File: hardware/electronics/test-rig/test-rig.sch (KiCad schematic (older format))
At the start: 59 parts, among them IC1 23LC1024, J1 JUMPER_OPEN, J2 JUMPER_CLOSED, J3 JUMPER_CLOSED, J4 AudioJack3_Ground, J5 Screw_Terminal_1x02, J6 Screw_Terminal_1x02, P1 CONN_01X15, P2 CONN_01X15, P3 CONN_01X04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

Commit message: Test rig
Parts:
- removed C14, C4, C5: 10u, symbol modular-internet-radio:CP_Small
- removed C24: 1u, symbol modular-internet-radio:C_Small
- removed L1, L2: Ferrite, symbol modular-internet-radio:Ferrite_Bead_Small
- added C14, C4, C5: 10u, Capacitors_SMD:C_0805_HandSoldering, symbol modular-internet-radio:C_Small
- C1, C10, C11, C12, C13, C16, C17, C18, C2, C20, C21, C3, C6, C7, C8, C9: footprint (none) -> Capacitors_SMD:C_0805_HandSoldering
- C15, C19, C22, C23: footprint (none) -> Capacitors_Tantalum_SMD:CP_Tantalum_Case-D_EIA-7343-31_Hand
- IC1: footprint DIL -> (none)
- P1, P2: footprint (none) -> Pin_Headers:Pin_Header_Straight_1x15_Pitch2.54mm
- P3, P4: footprint (none) -> Pin_Headers:Pin_Header_Straight_1x04_Pitch2.54mm
- P5, P6: footprint (none) -> Pin_Headers:Pin_Header_Straight_1x14_Pitch2.54mm
- P7: footprint (none) -> Pin_Headers:Pin_Header_Straight_1x01_Pitch2.54mm
- R1, R10, R11, R12, R13, R2, R3, R4, R5, R6, R7, R8, R9: footprint (none) -> Resistors_SMD:R_0805_HandSoldering
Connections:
- wire segments 300 -> 295
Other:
- note added: "+3.3V"
- note added: "AGND"
- note added: "AVDD"
- note added: "Ferrite"
- note added: "GND"
- note added: "Note 1: Removing the ferrite power decoupling (as in the Aadafruit design) and will try\n with partitioning of the ground and power planes."
- note added: "Note 2: Removed 1uF decoupling cap between AVDD and AGND (as per Adafruit\ndesign) as this covered by 10uF decoupling cap (as per manufacturer reference design)"
- note added: "See Note 1"
- note removed: "RESET JUMPER??"
- moved on the sheet: P2

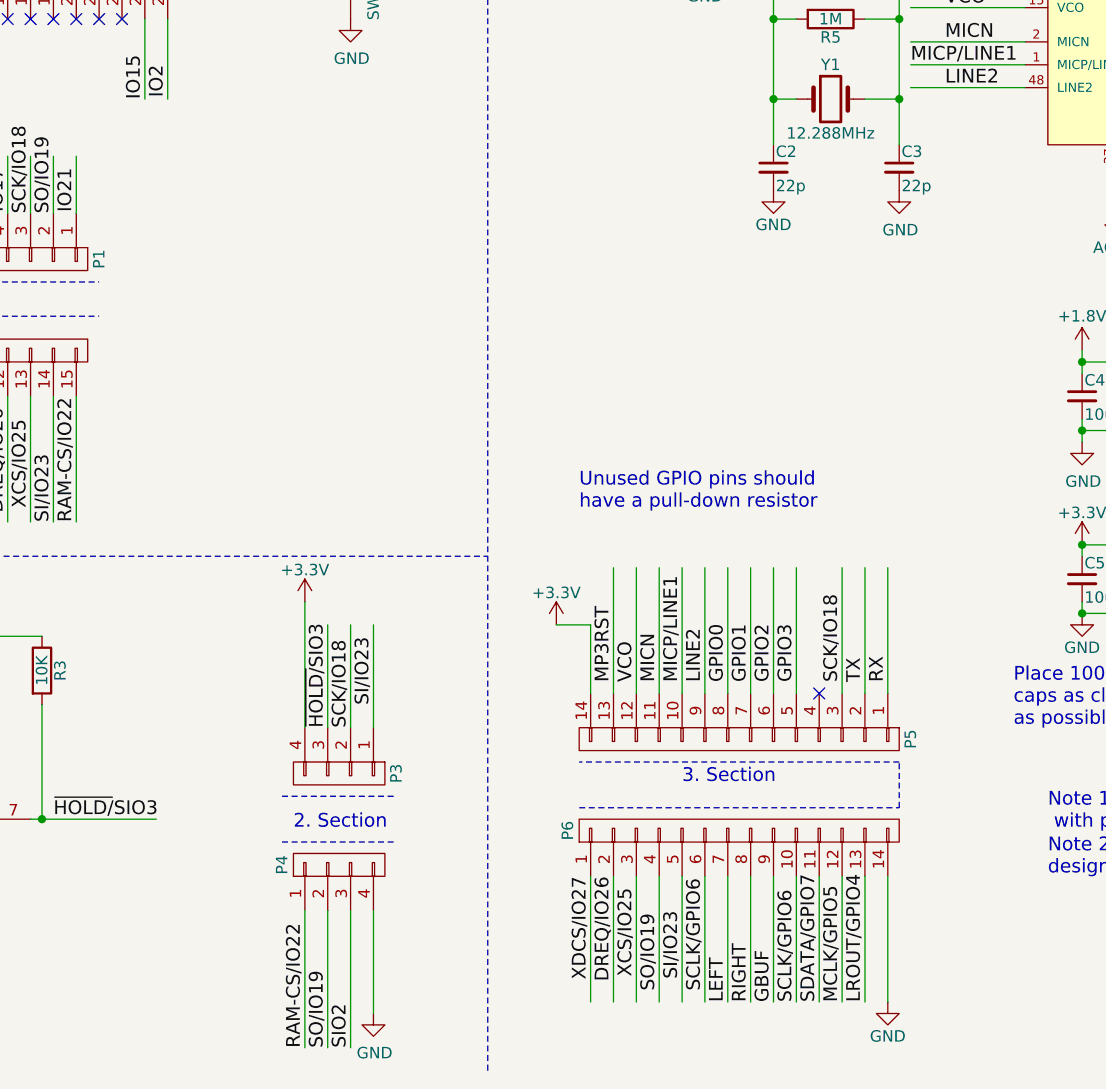
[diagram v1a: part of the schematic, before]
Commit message: Added programming header
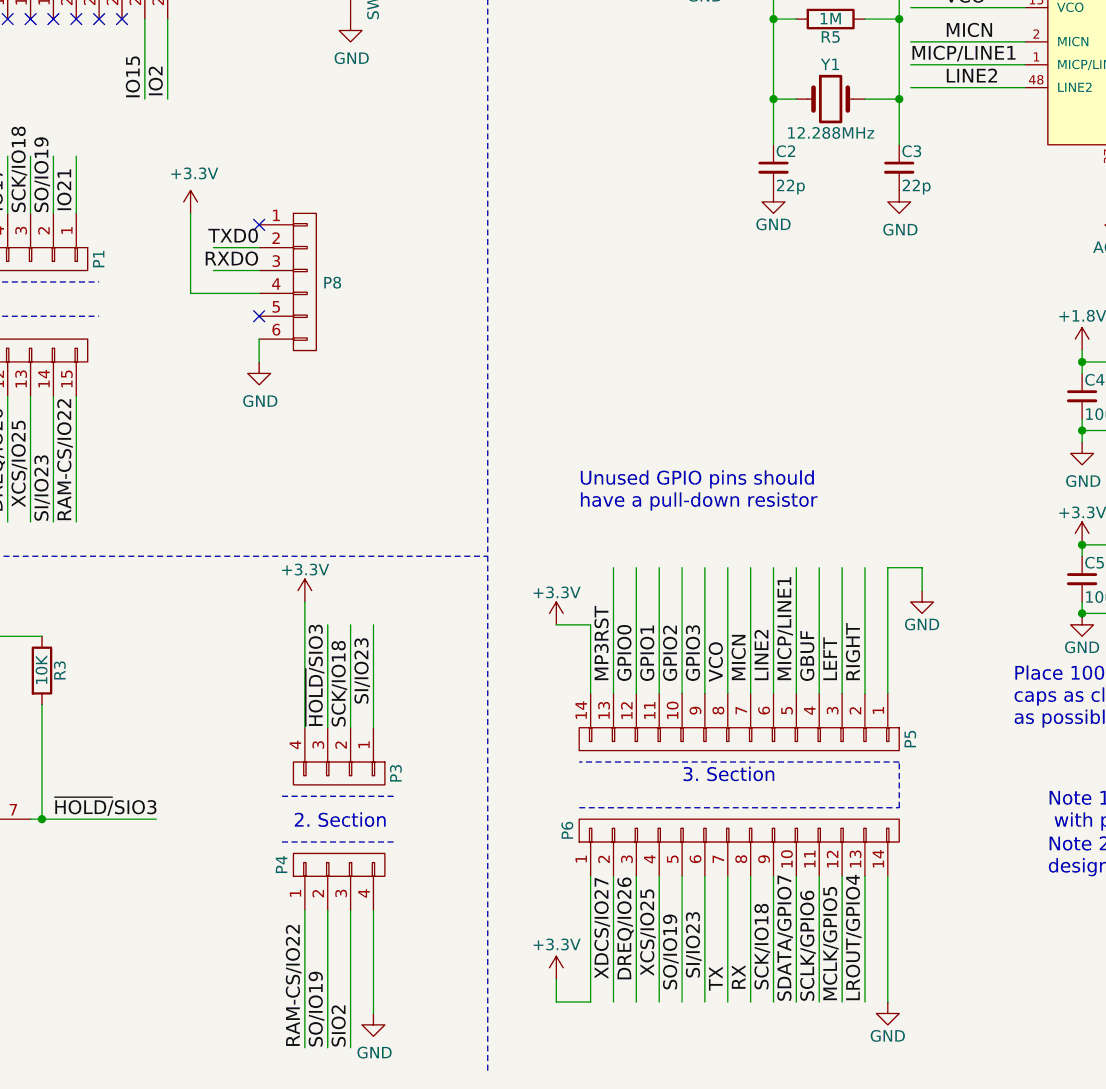
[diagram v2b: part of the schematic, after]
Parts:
- added P8: CONN_01X06, symbol conn:CONN_01X06
- U2: footprint LQFP48-0.5-7X7MM -> (none)
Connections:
- wire segments 295 -> 305
- no-connect marks 8 -> 9
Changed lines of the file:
@@
 F 0 "U2" H 6950 4350 50  0000 L BNN
 F 1 "VS1053B" H 7700 3100 50  0000 L BNN
-F 2 "LQFP48-0.5-7X7MM" H 7050 3200 50  0001 L BNN
+F 2 "" H 7050 3200 50  0001 L BNN
 F 3 "None" H 7100 3200 50  0001 L BNN
 F 4 "VLSI" H 7100 3200 50  0001 L BNN "Field4"
@@
 	1    0    0    -1
 $EndComp
-Text Label 5000 6950 3    60   ~ 0
+Text Label 5100 6950 3    60   ~ 0
 XDCS/IO27
-Text Label 5100 6950 3    60   ~ 0
+Text Label 5200 6950 3    60   ~ 0
 DREQ/IO26
-Text Label 5200 7000 3    60   ~ 0
+Text Label 5300 7000 3    60   ~ 0
 XCS/IO25
-Text Label 5300 7450 1    60   ~ 0
+Text Label 5400 7450 1    60   ~ 0
 SO/IO19
-Text Label 5400 7100 3    60   ~ 0
+Text Label 5500 7100 3    60   ~ 0
 SI/IO23
 Text Label 5100 6100 1    60   ~ 0
 MP3RST
-Text Label 5200 6100 1    60   ~ 0
+Text Label 5600 6100 1    60   ~ 0
 VCO
-Text Label 5300 6100 1    60   ~ 0
+Text Label 5700 6100 1    60   ~ 0
 MICN
-Text Label 5400 6100 1    60   ~ 0
+Text Label 5900 6100 1    60   ~ 0
 MICP/LINE1
-Text Label 5500 6100 1    60   ~ 0
+Text Label 5800 6100 1    60   ~ 0
 LINE2
-Text Label 6100 6100 1    60   ~ 0
+Text Label 5800 7450 1    60   ~ 0
 SCK/IO18
 Text Label 6200 7500 1    60   ~ 0
@@
 Text Label 6100 7500 1    60   ~ 0
 MCLK/GPIO5
-Text Label 5500 7450 1    60   ~ 0
-SCLK/GPIO6
+Text Label 5900 7500 1    60   ~ 0
+SDATA/GPIO7
+Text Label 5200 6100 1    60   ~ 0
+GPIO0
+Text Label 5300 6100 1    60   ~ 0
+GPIO1
+Text Label 5400 6100 1    60   ~ 0
+GPIO2
+Text Label 5500 6100 1    60   ~ 0
+GPIO3
+Text Label 6000 6100 1    60   ~ 0
+GBUF
+Text Label 6100 6100 1    60   ~ 0
+LEFT
+Text Label 6200 6100 1    60   ~ 0
+RIGHT
+Text Label 5600 7450 1    60   ~ 0
+TX
+Text Label 5700 7450 1    60   ~ 0
+RX
 Text Label 6000 7500 1    60   ~ 0
-SDATA/GPIO7
-Text Label 5600 6100 1    60   ~ 0
-GPIO0
-Text Label 5700 6100 1    60   ~ 0
-GPIO1
-Text Label 5800 6100 1    60   ~ 0
-GPIO2
-Text Label 5900 6100 1    60   ~ 0
-GPIO3
-Text Label 5800 7500 1    60   ~ 0
-GBUF
-Text Label 5600 7500 1    60   ~ 0
-LEFT
-Text Label 5700 7500 1    60   ~ 0
-RIGHT
-Text Label 6200 6100 1    60   ~ 0
-TX
-Text Label 6300 6100 1    60   ~ 0
-RX
-Text Label 5900 7500 1    60   ~ 0
 SCLK/GPIO6
 $Comp
@@
 	1    0    0    -1
 $EndComp
-NoConn ~ 6000 6150
 $Comp
 L modular-internet-radio:JUMPER_CLOSED J2
@@
 	1    0    0    -1
 $EndComp
+$Comp
+L conn:CONN_01X06 P8
+U 1 1 5DA474B9
+P 3750 4350
+F 0 "P8" H 3828 4345 50  0000 L CNN
+F 1 "CONN_01X06" H 3828 4300 50  0001 L CNN
+F 2 "" H 3750 4350 50  0001 C CNN
+F 3 "" H 3750 4350 50  0000 C CNN
+	1    3750 4350
+	1    0    0    -1
+$EndComp
+$Comp
+L modular-internet-radio:GND #PWR0101
+U 1 1 5DA48C32
+P 3550 4700
+F 0 "#PWR0101" H 3550 4450 50  0001 C CNN
+F 1 "GND" H 3555 4527 50  0000 C CNN
+F 2 "" H 3550 4700 50  0000 C CNN
+F 3 "" H 3550 4700 50  0000 C CNN
+	1    3550 4700
+	1    0    0    -1
+$EndComp
+Wire Wire Line
+	3550 4600 3550 4700
+$Comp
+L modular-internet-radio:+3.3V #PWR0102
+U 1 1 5DA606C5
+P 3250 4050
+F 0 "#PWR0102" H 3250 3900 50  0001 C CNN
+F 1 "+3.3V" H 3265 4223 50  0000 C CNN
+F 2 "" H 3250 4050 50  0000 C CNN
+F 3 "" H 3250 4050 50  0000 C CNN
+	1    3250 4050
+	1    0    0    -1
+$EndComp
+Wire Wire Line
+	3250 4050 3250 4400
+Wire Wire Line
+	3250 4400 3550 4400
+Wire Wire Line
+	3550 4300 3350 4300
+Wire Wire Line
+	3550 4200 3350 4200
+Text Label 3550 4300 2    60   ~ 0
+RXDO
+Text Label 3550 4200 2    60   ~ 0
+TXD0
+NoConn ~ 3550 4100
+NoConn ~ 3550 4500
+Wire Wire Line
+	6000 6150 6000 5600
+$Comp
+L modular-internet-radio:+3.3V #PWR0103
+U 1 1 5DAF44E9
+P 4850 7400
+F 0 "#PWR0103" H 4850 7250 50  0001 C CNN
+F 1 "+3.3V" H 4850 7550 50  0000 C CNN
+F 2 "" H 4850 7400 50  0000 C CNN
+F 3 "" H 4850 7400 50  0000 C CNN
+	1    4850 7400
+	1    0    0    -1
+$EndComp
+Wire Wire Line
+	4850 7400 4850 7500
+Wire Wire Line
+	4850 7500 5000 7500
+$Comp
+L modular-internet-radio:GND #PWR0104
+U 1 1 5DB0D1A5
+P 6450 5700
+F 0 "#PWR0104" H 6450 5450 50  0001 C CNN
+F 1 "GND" H 6450 5550 50  0000 C CNN
+F 2 "" H 6450 5700 50  0000 C CNN
+F 3 "" H 6450 5700 50  0000 C CNN
+	1    6450 5700
+	1    0    0    -1
+$EndComp
+Wire Wire Line
+	6300 5600 6450 5600
+Wire Wire Line
+	6450 5600 6450 5700
 $EndSCHEMATC

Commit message: failed-layout
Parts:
- removed J4: AudioJack3_Ground, symbol modular-internet-radio:AudioJack3_Ground
- added J4: AudioJack3_Switch, library:Stereo_Jack-Socket_6_Pin, symbol Connector:AudioJack3_Switch
- IC1: footprint (none) -> Housings_SOIC:SOIC-8_3.9x4.9mm_Pitch1.27mm
- J1: footprint (none) -> Jumper:SolderJumper-2_P1.3mm_Open_Pad1.0x1.5mm
- J2, J3: footprint (none) -> Jumper:SolderJumper-2_P1.3mm_Bridged_Pad1.0x1.5mm
- J5, J6: footprint (none) -> library:Screw_Terminal_1x02
- P8: footprint (none) -> Pin_Headers:Pin_Header_Straight_1x06_Pitch2.54mm
- SW1, SW2: footprint (none) -> library:SW-PUSH-RND-SMALL
- U1: footprint (none) -> library:ESP32-WROOM-32-Espressif-Symbol-Kicad-62379
- U2: footprint (none) -> Housings_QFP:LQFP-48_7x7mm_Pitch0.5mm
- U3: footprint (none) -> TO_SOT_Packages_SMD:SOT-223
- Y1: footprint (none) -> Crystals:Crystal_HC49-U_Vertical
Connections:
- wire segments 305 -> 302
- no-connect marks 9 -> 12
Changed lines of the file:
@@
 F 0 "IC1" H 1650 7250 50  0000 L CNN
 F 1 "23LC1024" H 1850 6500 50  0000 L CNN
-F 2 "" H 1750 6400 50  0001 C CIN
+F 2 "Housings_SOIC:SOIC-8_3.9x4.9mm_Pitch1.27mm" H 1750 6400 50  0001 C CIN
 F 3 "" H 2200 6300 50  0000 C CNN
 	1    2000 6800
@@
 F 0 "U2" H 6950 4350 50  0000 L BNN
 F 1 "VS1053B" H 7700 3100 50  0000 L BNN
-F 2 "" H 7050 3200 50  0001 L BNN
+F 2 "Housings_QFP:LQFP-48_7x7mm_Pitch0.5mm" H 7050 3200 50  0001 L BNN
 F 3 "None" H 7100 3200 50  0001 L BNN
 F 4 "VLSI" H 7100 3200 50  0001 L BNN "Field4"
@@
 F 0 "U1" H 2150 3050 60  0000 C CNN
 F 1 "ESP32-WROOM-32" H 2650 2750 60  0000 C CNN
-F 2 "" H 2750 1900 60  0001 C CNN
+F 2 "library:ESP32-WROOM-32-Espressif-Symbol-Kicad-62379" H 2750 1900 60  0001 C CNN
 F 3 "" H 2750 1900 60  0001 C CNN
 	1    2700 2000
@@
 F 0 "SW2" H 4000 3100 50  0000 L CNN
 F 1 "0" H 3950 2940 50  0000 C CNN
-F 2 "" H 3950 3200 50  0001 C CNN
+F 2 "library:SW-PUSH-RND-SMALL" H 3950 3200 50  0001 C CNN
 F 3 "" H 3950 3200 50  0001 C CNN
 	1    3950 3000
@@
 F 0 "Y1" H 6050 3700 50  0000 C CNN
 F 1 "12.288MHz" H 6050 3400 50  0000 C CNN
-F 2 "" H 6050 3550 50  0001 C CNN
+F 2 "Crystals:Crystal_HC49-U_Vertical" H 6050 3550 50  0001 C CNN
 F 3 "" H 6050 3550 50  0000 C CNN
 	1    6050 3550
@@
 F 0 "J6" H 11050 4050 50  0000 C TNN
 F 1 "Screw_Terminal_1x02" V 10900 3800 50  0001 C TNN
-F 2 "" H 11050 3575 50  0001 C CNN
+F 2 "library:Screw_Terminal_1x02" H 11050 3575 50  0001 C CNN
 F 3 "" H 11025 3800 50  0001 C CNN
 	1    11050 3800
@@
 F 0 "U3" H 8850 6075 50  0000 C CNN
 F 1 "LM1117-1.8" H 9000 6075 50  0000 L CNN
-F 2 "" H 9000 5950 50  0001 C CNN
+F 2 "TO_SOT_Packages_SMD:SOT-223" H 9000 5950 50  0001 C CNN
 F 3 "" H 9000 5950 50  0001 C CNN
 	1    9000 5950
 	1    0    0    -1
-$EndComp
-$Comp
-L modular-internet-radio:AudioJack3_Ground J4
-U 1 1 5D7E4362
-P 10900 4750
-F 0 "J4" H 10800 5000 50  0000 L TNN
-F 1 "AudioJack3_Ground" H 10900 5000 50  0001 C CNN
-F 2 "" H 10900 4750 50  0001 C CNN
-F 3 "" H 10900 4750 50  0001 C CNN
-	1    10900 4750
-	-1   0    0    1
 $EndComp
 $Comp
@@
 F 0 "J1" H 8100 1150 60  0000 C CNN
 F 1 "JUMPER_OPEN" H 8100 900 60  0001 C CNN
-F 2 "" H 8100 1250 60  0001 C CNN
+F 2 "Jumper:SolderJumper-2_P1.3mm_Open_Pad1.0x1.5mm" H 8100 1250 60  0001 C CNN
 F 3 "" H 8100 1250 60  0001 C CNN
 	1    8100 1000
@@
 F 0 "J5" H 11050 3450 50  0000 C TNN
 F 1 "Screw_Terminal_1x02" V 10900 3200 50  0001 C TNN
-F 2 "" H 11050 2975 50  0001 C CNN
+F 2 "library:Screw_Terminal_1x02" H 11050 2975 50  0001 C CNN
 F 3 "" H 11025 3200 50  0001 C CNN
 	1    11050 3200
@@
 L modular-internet-radio:AGND #PWR046
 U 1 1 5D81D88F
-P 10500 4900
-F 0 "#PWR046" H 10500 4650 50  0001 C CNN
-F 1 "AGND" H 10500 4750 50  0000 C CNN
-F 2 "" H 10500 4900 50  0000 C CNN
-F 3 "" H 10500 4900 50  0000 C CNN
-	1    10500 4900
+P 10200 4900
+F 0 "#PWR046" H 10200 4650 50  0001 C CNN
+F 1 "AGND" H 10200 4750 50  0000 C CNN
+F 2 "" H 10200 4900 50  0000 C CNN
+F 3 "" H 10200 4900 50  0000 C CNN
+	1    10200 4900
 	1    0    0    -1
 $EndComp
@@
 F 0 "SW1" H 850 1950 50  0000 L CNN
 F 1 "RST" H 800 1790 50  0000 C CNN
-F 2 "" H 800 2050 50  0001 C CNN
+F 2 "library:SW-PUSH-RND-SMALL" H 800 2050 50  0001 C CNN
 F 3 "" H 800 2050 50  0001 C CNN
 	1    800  1850
@@
 Text Label 2150 5400 1    60   ~ 0
 IO33
-Text Label 2050 5400 1    60   ~ 0
-IO35
 Text Notes 3700 6750 0    60   ~ 0
 2. Section
@@
 F 0 "J2" H 9350 3400 60  0000 C CNN
 F 1 "JUMPER_CLOSED" H 9350 3400 60  0001 C CNN
-F 2 "" H 9350 3750 60  0001 C CNN
+F 2 "Jumper:SolderJumper-2_P1.3mm_Bridged_Pad1.0x1.5mm" H 9350 3750 60  0001 C CNN
 F 3 "" H 9350 3750 60  0001 C CNN
 	1    9350 3500
-	1    0    0    -1
-$EndComp
-$Comp
-L modular-internet-radio:AGND #PWR050
-U 1 1 5D86148E
-P 11050 4300
-F 0 "#PWR050" H 11050 4050 50  0001 C CNN
-F 1 "AGND" H 11050 4150 50  0000 C CNN
-F 2 "" H 11050 4300 50  0000 C CNN
-F 3 "" H 11050 4300 50  0000 C CNN
-	1    11050 4300
 	1    0    0    -1
 $EndComp
@@
 F 0 "J3" H 9600 3500 60  0000 C CNN
 F 1 "JUMPER_CLOSED" H 9550 3300 60  0001 C CNN
-F 2 "" H 9550 3650 60  0001 C CNN
+F 2 "Jumper:SolderJumper-2_P1.3mm_Bridged_Pad1.0x1.5mm" H 9550 3650 60  0001 C CNN
 F 3 "" H 9550 3650 60  0001 C CNN
 	1    9550 3400
@@
 	10750 3100 10750 3400
 Connection ~ 10750 3400
-Wire Wire Line
-	10600 3700 10600 4750
 Connection ~ 10600 3700
 Wire Wire Line
@@
 	1950 4850 1950 5400
 Wire Wire Line
-	2050 4850 2050 5400
-Wire Wire Line
 	2150 4850 2150 5400
 Wire Wire Line
@@
 Wire Wire Line
 	9900 3500 9900 3700
-Wire Wire Line
-	10600 4750 10700 4750
-Wire Wire Line
-	10750 4400 10700 4400
-Wire Wire Line
-	10700 4400 10700 4650
-Wire Wire Line
-	10700 4850 10500 4850
-Wire Wire Line
-	10500 4850 10500 4900
-Wire Wire Line
-	10900 4450 10900 4300
-Wire Wire Line
-	10900 4300 11050 4300
 Wire Wire Line
 	8800 3500 9150 3500
@@
 F 0 "P8" H 3828 4345 50  0000 L CNN
 F 1 "CONN_01X06" H 3828 4300 50  0001 L CNN
-F 2 "" H 3750 4350 50  0001 C CNN
+F 2 "Pin_Headers:Pin_Header_Straight_1x06_Pitch2.54mm" H 3750 4350 50  0001 C CNN
 F 3 "" H 3750 4350 50  0000 C CNN
 	1    3750 4350
@@
 Wire Wire Line
 	6450 5600 6450 5700
+$Comp
+L Connector:AudioJack3_Switch J4
+U 1 1 5DA87EF9
+P 10600 4700
+F 0 "J4" V 10582 4320 50  0000 R CNN
+F 1 "AudioJack3_Switch" H 10582 5034 50  0001 C CNN
+F 2 "library:Stereo_Jack-Socket_6_Pin" H 10600 4700 50  0001 C CNN
+F 3 "~" H 10600 4700 50  0001 C CNN
+	1    10600 4700
+	0    -1   -1   0
+$EndComp
+Wire Wire Line
+	10200 4500 10400 4500
+Wire Wire Line
+	10200 4500 10200 4900
+Wire Wire Line
+	10600 3700 10600 4500
+Wire Wire Line
+	10750 4400 10800 4400
+Wire Wire Line
+	10800 4400 10800 4500
+NoConn ~ 10500 4500
+NoConn ~ 10700 4500
+NoConn ~ 10900 4500
+Wire Wire Line
+	2050 4850 2050 5350
+$Comp
+L modular-internet-radio:GND #PWR0105
+U 1 1 5DCA13D6
+P 2050 5350
+F 0 "#PWR0105" H 2050 5100 50  0001 C CNN
+F 1 "GND" H 2050 5200 50  0000 C CNN
+F 2 "" H 2050 5350 50  0000 C CNN
+F 3 "" H 2050 5350 50  0000 C CNN
+	1    2050 5350
+	1    0    0    -1
+$EndComp
 $EndSCHEMATC

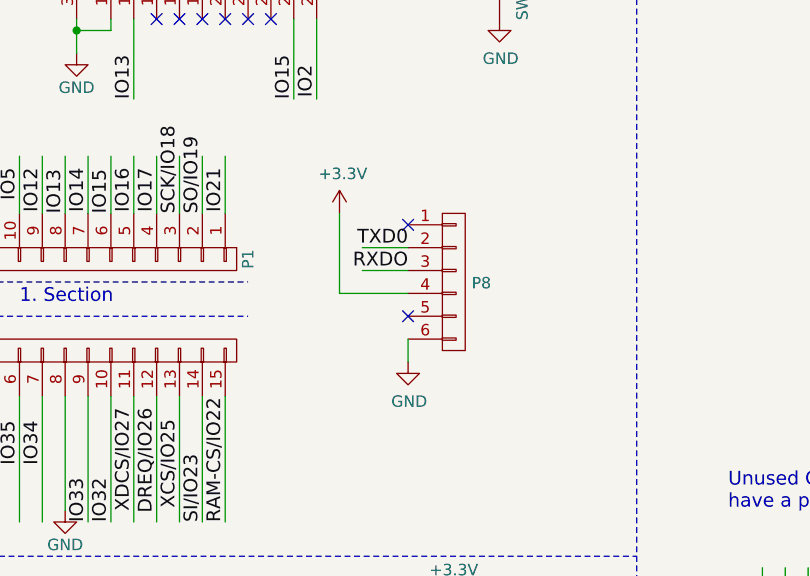
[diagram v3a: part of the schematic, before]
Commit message: WROOM and MEM layout completed
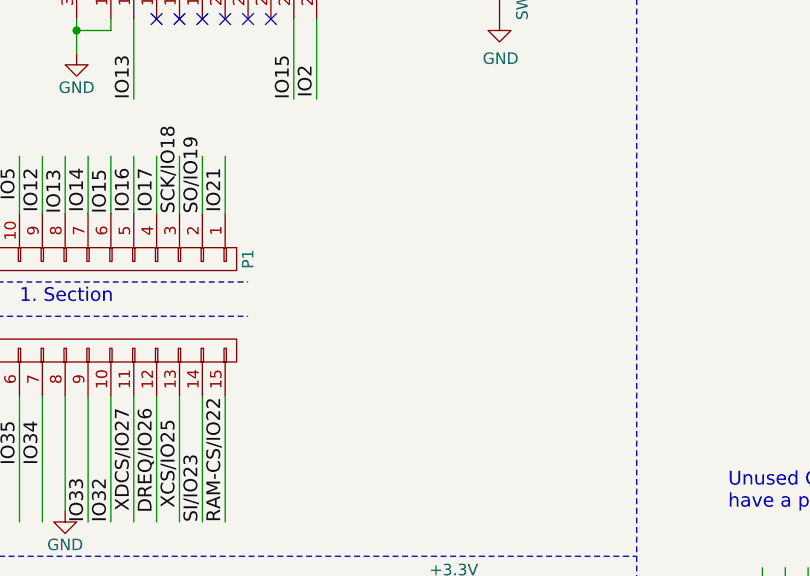
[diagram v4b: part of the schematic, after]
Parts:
- removed P8: CONN_01X06, Pin_Headers:Pin_Header_Straight_1x06_Pitch2.54mm, symbol conn:CONN_01X06
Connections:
- wire segments 302 -> 297
- no-connect marks 12 -> 10
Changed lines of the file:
@@
-	1    0    0    -1
-$EndComp
-$Comp
-L conn:CONN_01X06 P8
-U 1 1 5DA474B9
-P 3750 4350
-F 0 "P8" H 3828 4345 50  0000 L CNN
-F 1 "CONN_01X06" H 3828 4300 50  0001 L CNN
-F 2 "Pin_Headers:Pin_Header_Straight_1x06_Pitch2.54mm" H 3750 4350 50  0001 C CNN
-F 3 "" H 3750 4350 50  0000 C CNN
-	1    3750 4350
-	1    0    0    -1
-$EndComp
-$Comp
-L modular-internet-radio:GND #PWR0101
-U 1 1 5DA48C32
-P 3550 4700
-F 0 "#PWR0101" H 3550 4450 50  0001 C CNN
-F 1 "GND" H 3555 4527 50  0000 C CNN
-F 2 "" H 3550 4700 50  0000 C CNN
-F 3 "" H 3550 4700 50  0000 C CNN
-	1    3550 4700
 	1    0    0    -1
 $EndComp
 Wire Wire Line
-	3550 4600 3550 4700
-$Comp
-L modular-internet-radio:+3.3V #PWR0102
-U 1 1 5DA606C5
-P 3250 4050
-F 0 "#PWR0102" H 3250 3900 50  0001 C CNN
-F 1 "+3.3V" H 3265 4223 50  0000 C CNN
-F 2 "" H 3250 4050 50  0000 C CNN
-F 3 "" H 3250 4050 50  0000 C CNN
-	1    3250 4050
-	1    0    0    -1
-$EndComp
-Wire Wire Line
-	3250 4050 3250 4400
-Wire Wire Line
-	3250 4400 3550 4400
-Wire Wire Line
-	3550 4300 3350 4300
-Wire Wire Line
-	3550 4200 3350 4200
-Text Label 3550 4300 2    60   ~ 0
-RXDO
-Text Label 3550 4200 2    60   ~ 0
-TXD0
-NoConn ~ 3550 4100
-NoConn ~ 3550 4500
-Wire Wire Line
 	6000 6150 6000 5600
